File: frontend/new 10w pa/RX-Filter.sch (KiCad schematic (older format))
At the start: 83 parts, among them U5 TPIC6B595, U6 TPIC6B595

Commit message: Minor updates to v1.12
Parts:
- added C78, C79: 150pF, Capacitors_SMD:C_0805, symbol C
- added P9: CONN_02X05, Pin_Headers:Pin_Header_Straight_2x05, symbol CONN_02X05
- C57, C68: value 300pF -> 150pF
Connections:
- net labels added: ANT1, ANT2, ANT3
- wire segments 108 -> 141
- no-connect marks 10 -> 3
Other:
- note added: "Pin 1 = 20 db Pin 2 = Bypass\nPin 3 = 10 db Pin 4 = Rx IN\nPin 5 = ANT 1 Pin 6 = RX 1\nPin 7 = ANT 2 Pin 8 = RX 2\nPin 9 = ANT3 Pin 10 = XV Rx IN"
- note added: "This is an optional connector to allow access and \nexternal control of off-board circuitry as outlined\nin the Alex Control Specification."
- moved on the sheet: C47, C52, C57, C72, D9, L18, L23, L37

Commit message: Starting Layout
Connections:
- wire segments 141 -> 140
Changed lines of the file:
@@
 Connection ~ 2100 4350
 Wire Wire Line
-	2800 4350 2850 4350
+	2800 4350 3200 4350
 Wire Wire Line
 	1550 3950 2150 3950
@@
 $EndComp
 Wire Wire Line
-	2900 4350 3200 4350
-Wire Wire Line
 	3200 4350 3200 4450

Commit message: Continuing board routing
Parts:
- removed D4: RED, LEDs:LED-1206, symbol LED
- removed D5: YEL, LEDs:LED-1206, symbol LED
- removed R13, R14: 1k, Resistors_SMD:R_0805, symbol R
- C43, C44, C45, C46, C47, C48, C49, C50, C51, C52, C53, C54, C55, C56, C57, C58, C59, C60, C61, C62, C63, C64, C65, C66, C67, C68, C69, C70, C71, C72, C73, C74, C75, C76, C77, C78, C79: footprint Capacitors_SMD:C_0805 -> HERMESLITE:C_0805
- L14, L15, L16, L17, L18, L19, L20, L21, L22, L23, L24, L25, L26, L27, L28, L29, L30, L31, L32, L33, L34, L35, L36, L37, L38: footprint Choke_SMD:Choke_SMD_1206_Standard -> HERMESLITE:Choke_SMD_1206_Standard
- R15, R16, R17, R18, R19: footprint Resistors_SMD:R_0805 -> HERMESLITE:R_0805
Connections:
- wire segments 140 -> 132
- no-connect marks 3 -> 5

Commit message: More pcb changes
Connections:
- net RX-IN: now also C77.1; no longer C43.2
- net RX-OUT: now also C43.2; no longer C77.1
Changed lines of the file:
@@
 Comment4 ""
 $EndDescr
-Text GLabel 2150 1300 0    50   Input ~ 0
+Text GLabel 9000 1300 2    50   Input ~ 0
 RX-IN
-Text GLabel 9000 1300 2    50   Output ~ 0
+Text GLabel 2150 1300 0    50   Output ~ 0
 RX-OUT
 $Comp
@@
 	2150 3950 2150 4000
 $Comp
-L GND #PWR046
+L GND #PWR047
 U 1 1 54A23178
 P 2150 4000
-F 0 "#PWR046" H 2150 4000 30  0001 C CNN
+F 0 "#PWR047" H 2150 4000 30  0001 C CNN
 F 1 "GND" H 2150 3930 30  0001 C CNN
 F 2 "" H 2150 4000 60  0000 C CNN
@@
 	2150 5650 2150 5700
 $Comp
-L GND #PWR047
+L GND #PWR048
 U 1 1 54A23184
 P 2150 5700
-F 0 "#PWR047" H 2150 5700 30  0001 C CNN
+F 0 "#PWR048" H 2150 5700 30  0001 C CNN
 F 1 "GND" H 2150 5630 30  0001 C CNN
 F 2 "" H 2150 5700 60  0000 C CNN
@@
 $EndComp
 $Comp
-L GND #PWR048
+L GND #PWR049
 U 1 1 54A26D4B
 P 7800 2700
-F 0 "#PWR048" H 7800 2700 30  0001 C CNN
+F 0 "#PWR049" H 7800 2700 30  0001 C CNN
 F 1 "GND" H 7800 2630 30  0001 C CNN
 F 2 "" H 7800 2700 50  0000 C CNN
@@
 $EndComp
 $Comp
-L GND #PWR049
+L GND #PWR050
 U 1 1 54A26D51
 P 6550 2700
-F 0 "#PWR049" H 6550 2700 30  0001 C CNN
+F 0 "#PWR050" H 6550 2700 30  0001 C CNN
 F 1 "GND" H 6550 2630 30  0001 C CNN
 F 2 "" H 6550 2700 50  0000 C CNN
@@
 $EndComp
 $Comp
-L GND #PWR050
+L GND #PWR051
 U 1 1 54A26D57
 P 6300 2900
-F 0 "#PWR050" H 6300 2900 30  0001 C CNN
+F 0 "#PWR051" H 6300 2900 30  0001 C CNN
 F 1 "GND" H 6300 2830 30  0001 C CNN
 F 2 "" H 6300 2900 50  0000 C CNN
@@
 $EndComp
 $Comp
-L GND #PWR051
+L GND #PWR052
 U 1 1 54A26D5D
 P 5300 2700
-F 0 "#PWR051" H 5300 2700 30  0001 C CNN
+F 0 "#PWR052" H 5300 2700 30  0001 C CNN
 F 1 "GND" H 5300 2630 30  0001 C CNN
 F 2 "" H 5300 2700 50  0000 C CNN
@@
 $EndComp
 $Comp
-L GND #PWR052
+L GND #PWR053
 U 1 1 54A26D72
 P 4650 3000
-F 0 "#PWR052" H 4650 3000 30  0001 C CNN
+F 0 "#PWR053" H 4650 3000 30  0001 C CNN
 F 1 "GND" H 4650 2930 30  0001 C CNN
 F 2 "" H 4650 3000 50  0000 C CNN
@@
 $EndComp
 $Comp
-L GND #PWR053
+L GND #PWR054
 U 1 1 54A26D78
 P 7950 3000
-F 0 "#PWR053" H 7950 3000 30  0001 C CNN
+F 0 "#PWR054" H 7950 3000 30  0001 C CNN
 F 1 "GND" H 7950 2930 30  0001 C CNN
 F 2 "" H 7950 3000 50  0000 C CNN
@@
 $EndComp
 $Comp
-L GND #PWR054
+L GND #PWR055
 U 1 1 54A28AFC
 P 7800 4700
-F 0 "#PWR054" H 7800 4700 30  0001 C CNN
+F 0 "#PWR055" H 7800 4700 30  0001 C CNN
 F 1 "GND" H 7800 4630 30  0001 C CNN
 F 2 "" H 7800 4700 50  0000 C CNN
@@
 $EndComp
 $Comp
-L GND #PWR055
+L GND #PWR056
 U 1 1 54A28B02
 P 6550 4700
-F 0 "#PWR055" H 6550 4700 30  0001 C CNN
+F 0 "#PWR056" H 6550 4700 30  0001 C CNN
 F 1 "GND" H 6550 4630 30  0001 C CNN
 F 2 "" H 6550 4700 50  0000 C CNN
@@
 $EndComp
 $Comp
-L GND #PWR056
+L GND #PWR057
 U 1 1 54A28B08
 P 6300 4900
-F 0 "#PWR056" H 6300 4900 30  0001 C CNN
+F 0 "#PWR057" H 6300 4900 30  0001 C CNN
 F 1 "GND" H 6300 4830 30  0001 C CNN
 F 2 "" H 6300 4900 50  0000 C CNN
@@
 $EndComp
 $Comp
-L GND #PWR057
+L GND #PWR058
 U 1 1 54A28B0E
 P 5300 4700
-F 0 "#PWR057" H 5300 4700 30  0001 C CNN
+F 0 "#PWR058" H 5300 4700 30  0001 C CNN
 F 1 "GND" H 5300 4630 30  0001 C CNN
 F 2 "" H 5300 4700 50  0000 C CNN
@@
 $EndComp
 $Comp
-L GND #PWR058
+L GND #PWR059
 U 1 1 54A28B21
 P 4650 5000
-F 0 "#PWR058" H 4650 5000 30  0001 C CNN
+F 0 "#PWR059" H 4650 5000 30  0001 C CNN
 F 1 "GND" H 4650 4930 30  0001 C CNN
 F 2 "" H 4650 5000 50  0000 C CNN
@@
 $EndComp
 $Comp
-L GND #PWR059
+L GND #PWR060
 U 1 1 54A28B27
 P 7950 5000
-F 0 "#PWR059" H 7950 5000 30  0001 C CNN
+F 0 "#PWR060" H 7950 5000 30  0001 C CNN
 F 1 "GND" H 7950 4930 30  0001 C CNN
 F 2 "" H 7950 5000 50  0000 C CNN
@@
 $EndComp
 $Comp
-L GND #PWR060
+L GND #PWR061
 U 1 1 54A2A84A
 P 7800 3700
-F 0 "#PWR060" H 7800 3700 30  0001 C CNN
+F 0 "#PWR061" H 7800 3700 30  0001 C CNN
 F 1 "GND" H 7800 3630 30  0001 C CNN
 F 2 "" H 7800 3700 50  0000 C CNN
@@
 $EndComp
 $Comp
-L GND #PWR061
+L GND #PWR062
 U 1 1 54A2A850
 P 6550 3700
-F 0 "#PWR061" H 6550 3700 30  0001 C CNN
+F 0 "#PWR062" H 6550 3700 30  0001 C CNN
 F 1 "GND" H 6550 3630 30  0001 C CNN
 F 2 "" H 6550 3700 50  0000 C CNN
@@
 $EndComp
 $Comp
-L GND #PWR062
+L GND #PWR063
 U 1 1 54A2A856
 P 6300 3900
-F 0 "#PWR062" H 6300 3900 30  0001 C CNN
+F 0 "#PWR063" H 6300 3900 30  0001 C CNN
 F 1 "GND" H 6300 3830 30  0001 C CNN
 F 2 "" H 6300 3900 50  0000 C CNN
@@
 $EndComp
 $Comp
-L GND #PWR063
+L GND #PWR064
 U 1 1 54A2A85C
 P 5300 3700
-F 0 "#PWR063" H 5300 3700 30  0001 C CNN
+F 0 "#PWR064" H 5300 3700 30  0001 C CNN
 F 1 "GND" H 5300 3630 30  0001 C CNN
 F 2 "" H 5300 3700 50  0000 C CNN
@@
 $EndComp
 $Comp
-L GND #PWR064
+L GND #PWR065
 U 1 1 54A2A86F
 P 4650 4000
-F 0 "#PWR064" H 4650 4000 30  0001 C CNN
+F 0 "#PWR065" H 4650 4000 30  0001 C CNN
 F 1 "GND" H 4650 3930 30  0001 C CNN
 F 2 "" H 4650 4000 50  0000 C CNN
@@
 $EndComp
 $Comp
-L GND #PWR065
+L GND #PWR066
 U 1 1 54A2A875
 P 7950 4000
-F 0 "#PWR065" H 7950 4000 30  0001 C CNN
+F 0 "#PWR066" H 7950 4000 30  0001 C CNN
 F 1 "GND" H 7950 3930 30  0001 C CNN
 F 2 "" H 7950 4000 50  0000 C CNN
@@
 $EndComp
 $Comp
-L GND #PWR066
+L GND #PWR067
 U 1 1 54A2AFAC
 P 7800 5700
-F 0 "#PWR066" H 7800 5700 30  0001 C CNN
+F 0 "#PWR067" H 7800 5700 30  0001 C CNN
 F 1 "GND" H 7800 5630 30  0001 C CNN
 F 2 "" H 7800 5700 50  0000 C CNN
@@
 $EndComp
 $Comp
-L GND #PWR067
+L GND #PWR068
 U 1 1 54A2AFB2
 P 6550 5700
-F 0 "#PWR067" H 6550 5700 30  0001 C CNN
+F 0 "#PWR068" H 6550 5700 30  0001 C CNN
 F 1 "GND" H 6550 5630 30  0001 C CNN
 F 2 "" H 6550 5700 50  0000 C CNN
@@
 $EndComp
 $Comp
-L GND #PWR068
+L GND #PWR069
 U 1 1 54A2AFB8
 P 6300 5900
-F 0 "#PWR068" H 6300 5900 30  0001 C CNN
+F 0 "#PWR069" H 6300 5900 30  0001 C CNN
 F 1 "GND" H 6300 5830 30  0001 C CNN
 F 2 "" H 6300 5900 50  0000 C CNN
@@
 $EndComp
 $Comp
-L GND #PWR069
+L GND #PWR070
 U 1 1 54A2AFBE
 P 5200 5700
-F 0 "#PWR069" H 5200 5700 30  0001 C CNN
+F 0 "#PWR070" H 5200 5700 30  0001 C CNN
 F 1 "GND" H 5200 5630 30  0001 C CNN
 F 2 "" H 5200 5700 50  0000 C CNN
@@
 $EndComp
 $Comp
-L GND #PWR070
+L GND #PWR071
 U 1 1 54A2AFD1
 P 4600 6000
-F 0 "#PWR070" H 4600 6000 30  0001 C CNN
+F 0 "#PWR071" H 4600 6000 30  0001 C CNN
 F 1 "GND" H 4600 5930 30  0001 C CNN
 F 2 "" H 4600 6000 50  0000 C CNN
@@
 $EndComp
 $Comp
-L GND #PWR071
+L GND #PWR072
 U 1 1 54A2AFD7
 P 8050 6000
-F 0 "#PWR071" H 8050 6000 30  0001 C CNN
+F 0 "#PWR072" H 8050 6000 30  0001 C CNN
 F 1 "GND" H 8050 5930 30  0001 C CNN
 F 2 "" H 8050 6000 50  0000 C CNN
@@
 $EndComp
 $Comp
-L GND #PWR072
+L GND #PWR073
 U 1 1 54A2CBBC
 P 6550 6700
-F 0 "#PWR072" H 6550 6700 30  0001 C CNN
+F 0 "#PWR073" H 6550 6700 30  0001 C CNN
 F 1 "GND" H 6550 6630 30  0001 C CNN
 F 2 "" H 6550 6700 50  0000 C CNN
@@
 $EndComp
 $Comp
-L GND #PWR073
+L GND #PWR074
 U 1 1 54A2CBCE
 P 5300 6700
-F 0 "#PWR073" H 5300 6700 30  0001 C CNN
+F 0 "#PWR074" H 5300 6700 30  0001 C CNN
 F 1 "GND" H 5300 6630 30  0001 C CNN
 F 2 "" H 5300 6700 50  0000 C CNN
@@
 $EndComp
 $Comp
-L GND #PWR074
+L GND #PWR075
 U 1 1 54A2CBE1
 P 4650 7000
-F 0 "#PWR074" H 4650 7000 30  0001 C CNN
+F 0 "#PWR075" H 4650 7000 30  0001 C CNN
 F 1 "GND" H 4650 6930 30  0001 C CNN
 F 2 "" H 4650 7000 50  0000 C CNN
@@
 $EndComp
 $Comp
-L GND #PWR075
+L GND #PWR076
 U 1 1 54A2CBE7
 P 6700 7000
-F 0 "#PWR075" H 6700 7000 30  0001 C CNN
+F 0 "#PWR076" H 6700 7000 30  0001 C CNN
 F 1 "GND" H 6700 6930 30  0001 C CNN
 F 2 "" H 6700 7000 50  0000 C CNN

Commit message: BCD Filter update
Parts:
- removed P9: CONN_02X05, Pin_Headers:Pin_Header_Straight_2x05, symbol CONN_02X05
- removed U5, U6: TPIC6B595, Housings_SOIC:SOIC-20_7.5x12.8mm_Pitch1.27mm, symbol TPIC6B595
- added Q10, Q11, Q12, Q13, Q14: 2N7000, SMD_Packages:SOT-23-GDS, symbol MOSFET_N
- added U2: 4028, SMD_Packages:TSSOP-16, symbol 4028
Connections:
- net GND: now also Q10.S, Q11.S, Q12.S, Q13.S, Q14.S, U2.16 (VDD)
- net at C46.1, C71.1, L17.2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: now also Q12.D
- net at C47.1, C72.1, L18.2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: now also Q13.D
- net at C48.1, C59.1, L19.2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: now also Q14.D
- net at C45.1, C70.1, L16.2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: now also Q11.D
- net at C44.1, C69.1, L15.2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: now also Q10.D
- new net: Q10.G, U2.6 (S5)
- new net: Q11.G, U2.1 (S4)
- new net: Q14.G, U2.14 (S1)
- new net: Q12.G, U2.15 (S3)
- new net: Q13.G, U2.2 (S2)
- new net A: U2.10 (A)
- new net B: U2.13 (B)
- new net C: U2.12 (C)
- new net PTT: U2.11 (D)
- new net VSS: U2.8 (VSS)
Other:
- note added: "#PTT is inverted to PTT and is \nused to enable/disable RX. \nWhen PTT is low, valid ouputs\nexist on S1 thru S5"
- note added: "Filter Settings for PowerSDR Hermes Ctrl\n(set for RX J16 Pins only)\n 1 2 3 4-7=Don't Care\n160M 1 0 0\n80M 0 1 0\n60M 0 1 0\n40M 1 1 0\n30M 1 1 0\n20M 0 0 1\n17M 0 0 1\n15M 1 0 1\n12M 1 0 1\n10M 1 0 1\nRest 1 1 1"
- note removed: "Pin 1 = 20 db Pin 2 = Bypass\nPin 3 = 10 db Pin 4 = Rx IN\nPin 5 = ANT 1 Pin 6 = RX 1\nPin 7 = ANT 2 Pin 8 = RX 2\nPin 9 = ANT3 Pin 10 = XV Rx IN"
- note removed: "This is an optional connector to allow access and \nexternal control of off-board circuitry as outlined\nin the Alex Control Specification."

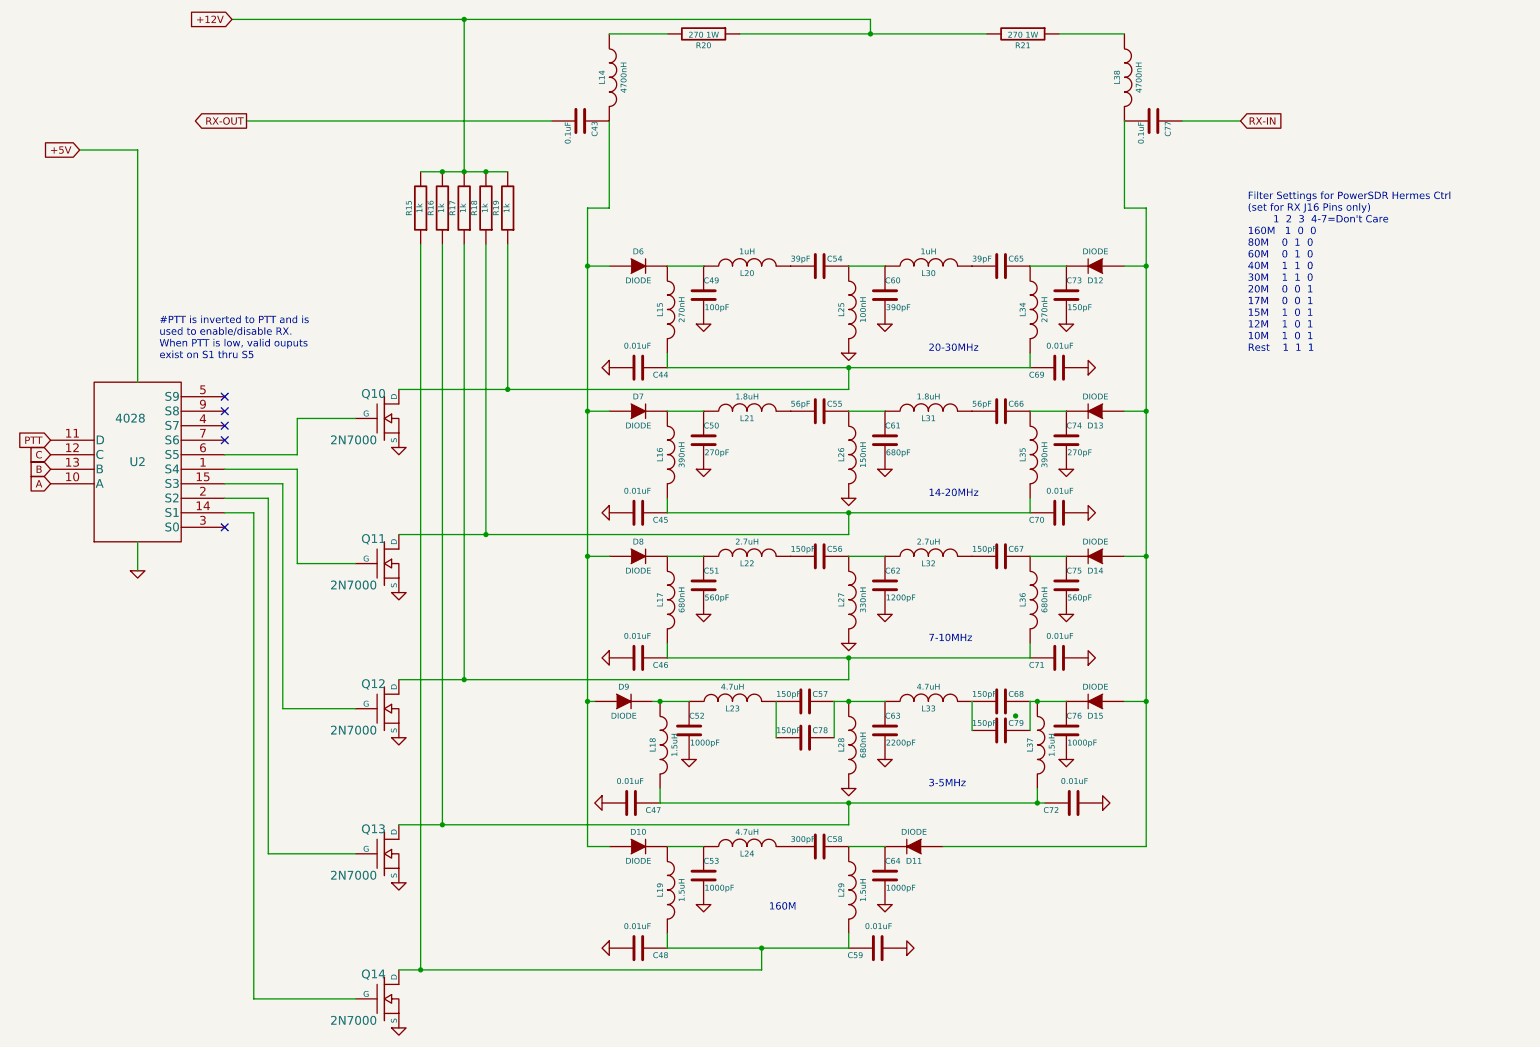
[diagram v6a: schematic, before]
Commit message: Changes for new J16 approach
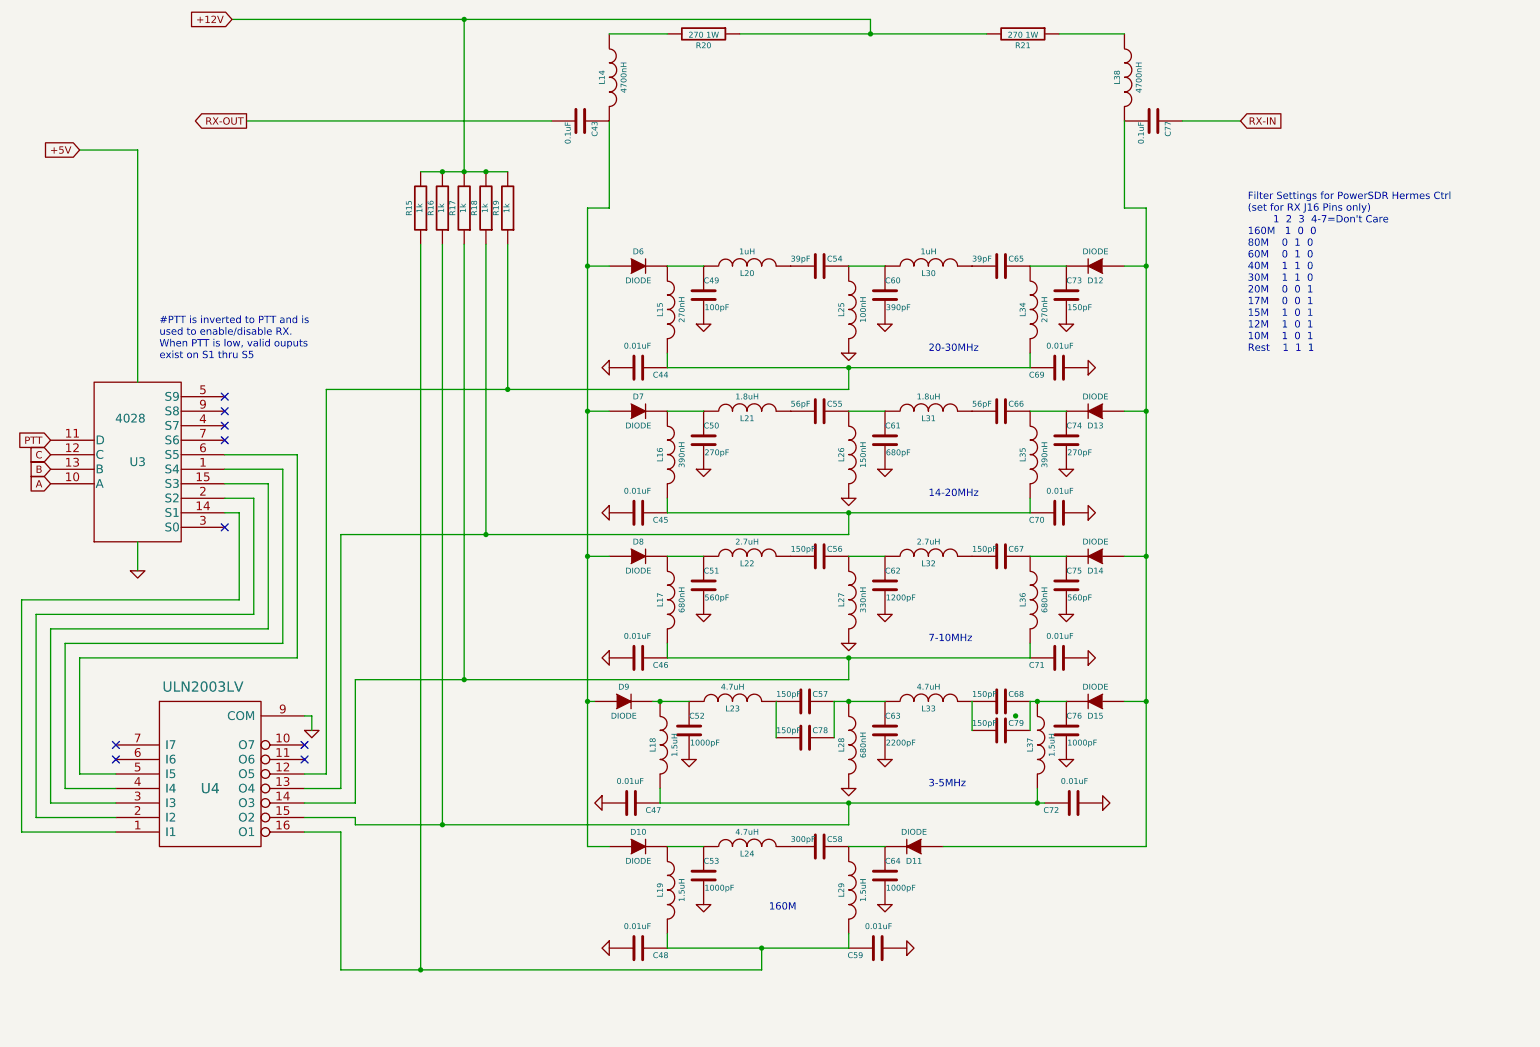
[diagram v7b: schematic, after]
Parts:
- removed Q10, Q11, Q12, Q13, Q14: 2N7000, SMD_Packages:SOT-23-GDS, symbol MOSFET_N
- added U4: ULN2003LV, SMD_Packages:TSSOP-16, symbol ULN2003A
- renumbered U2 to U3
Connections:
- net GND: now also U4.8 (GND), U4.9 (COM)
- net at C44.1, C69.1, L15.2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: now also U4.12 (O5)
- net at C46.1, C71.1, L17.2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: now also U4.14 (O3)
- net at C45.1, C70.1, L16.2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: now also U4.13 (O4)
- net at C47.1, C72.1, L18.2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: now also U4.15 (O2)
- net at C48.1, C59.1, L19.2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: now also U4.16 (O1)
- net at U3.6 (S5): now also U4.5 (I5)
- net at U3.1 (S4): now also U4.4 (I4)
- net at U3.14 (S1): now also U4.1 (I1)
- net at U3.15 (S3): now also U4.3 (I3)
- net at U3.2 (S2): now also U4.2 (I2)
- no-connect marks 5 -> 9

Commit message: Final pcd changes
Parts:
- removed U3: 4028, SMD_Packages:TSSOP-16, symbol 4028
- removed U4: ULN2003LV, SMD_Packages:TSSOP-16, symbol ULN2003A
- added C83: 1000pF, HERMESLITE:C_0805, symbol C
- added C84, C85: 0.01uF, HERMESLITE:C_0805, symbol C
- added D1, D16, D17, D2, D3, D4, D5: DIODE, Diodes_SMD:Diode-SMA_Standard, symbol DIODE
- added L39: 4700nH, HERMESLITE:Choke_SMD_1206_Standard, symbol INDUCTOR
- added L40: 4700uH, HERMESLITE:Choke_SMD_1206_Standard, symbol INDUCTOR
- added Q4: 2N7000, SMD_Packages:SOT-23-GDS, symbol MOS_N
- added R13, R14: 1k, HERMESLITE:R_0805, symbol R
- added U3: 74LS145, Housings_SOIC:SOIC-16_3.9x9.9mm_Pitch1.27mm, symbol 74LS145
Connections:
- net +12V: now also R13.2, R14.2
- net A: now also U3.15 (P0)
- net B: now also U3.14 (P1)
- net C: now also U3.13 (P2)
- net GND: now also C84.2, C85.2, Q4.S, U3.8 (GND)
- net at C43.1, D10.1 (A), D6.1 (A)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: now also D16.1 (A)
- net at C77.2, D11.1 (A), D12.1 (A)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: now also D17.1 (A)
- net at C44.1, C69.1, L15.2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: now also D5.2 (K), U3.10 (Q8), U3.11 (Q9), U3.7 (Q6), U3.9 (Q7)
- net at C46.1, C71.1, L17.2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: now also D3.2 (K), U3.4 (Q3), U3.5 (Q4)
- net at C45.1, C70.1, L16.2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: now also D4.2 (K), U3.6 (Q5)
- net at C47.1, C72.1, L18.2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: now also D2.2 (K), U3.2 (Q1), U3.3 (Q2)
- net at C48.1, C59.1, L19.2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: now also D1.2 (K), U3.1 (Q0)
- new net: C83.2, D16.2 (K), L39.1
- new net: C83.1, D17.2 (K), L40.1
- new net: C84.1, C85.1, L39.2, L40.2, Q4.D, R14.1
- new net: D1.1 (A), D2.1 (A), D3.1 (A), D4.1 (A), D5.1 (A), Q4.G, R13.1
- new net D: U3.12 (P3)
- new net VCC: U3.16 (VCC)
- no-connect marks 9 -> 0
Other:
- note added: "Bypass"
- note added: "Filter Settings for PowerSDR Hermes Ctrl\n(set for RX and TX J16 Pins)\n 1 2 3 4 \nBypass 0 1 0 1 (or higher) \n160M 0 0 0 0\n80M 1 0 0 0\n60M 0 1 0 0\n40M 1 1 0 0\n30M 0 0 1 0\n20M 1 0 1 0\n17M 0 1 1 0\n15M 1 1 1 0\n12M 0 0 0 1\n10M 1 0 0 1"
- note removed: "#PTT is inverted to PTT and is \nused to enable/disable RX. \nWhen PTT is low, valid ouputs\nexist on S1 thru S5"
- note removed: "Filter Settings for PowerSDR Hermes Ctrl\n(set for RX J16 Pins only)\n 1 2 3 4-7=Don't Care\n160M 1 0 0\n80M 0 1 0\n60M 0 1 0\n40M 1 1 0\n30M 1 1 0\n20M 0 0 1\n17M 0 0 1\n15M 1 0 1\n12M 1 0 1\n10M 1 0 1\nRest 1 1 1"
